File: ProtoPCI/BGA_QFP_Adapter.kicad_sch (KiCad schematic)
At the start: 2 parts

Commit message: Initial BGA to QFP Adapter for QFP replacement via BGA
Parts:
- U2: footprint Package_QFP:PQFP-160_28x28mm_P0.65mm -> DFT:DFT_PQFP-160_28x28mm_P0.65mm_Adapter
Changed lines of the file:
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@@
 			)
 		)
-		(property "Footprint" "Package_QFP:PQFP-160_28x28mm_P0.65mm"
+		(property "Footprint" "DFT:DFT_PQFP-160_28x28mm_P0.65mm_Adapter"
 			(at 147.32 92.71 0)
 			(effects

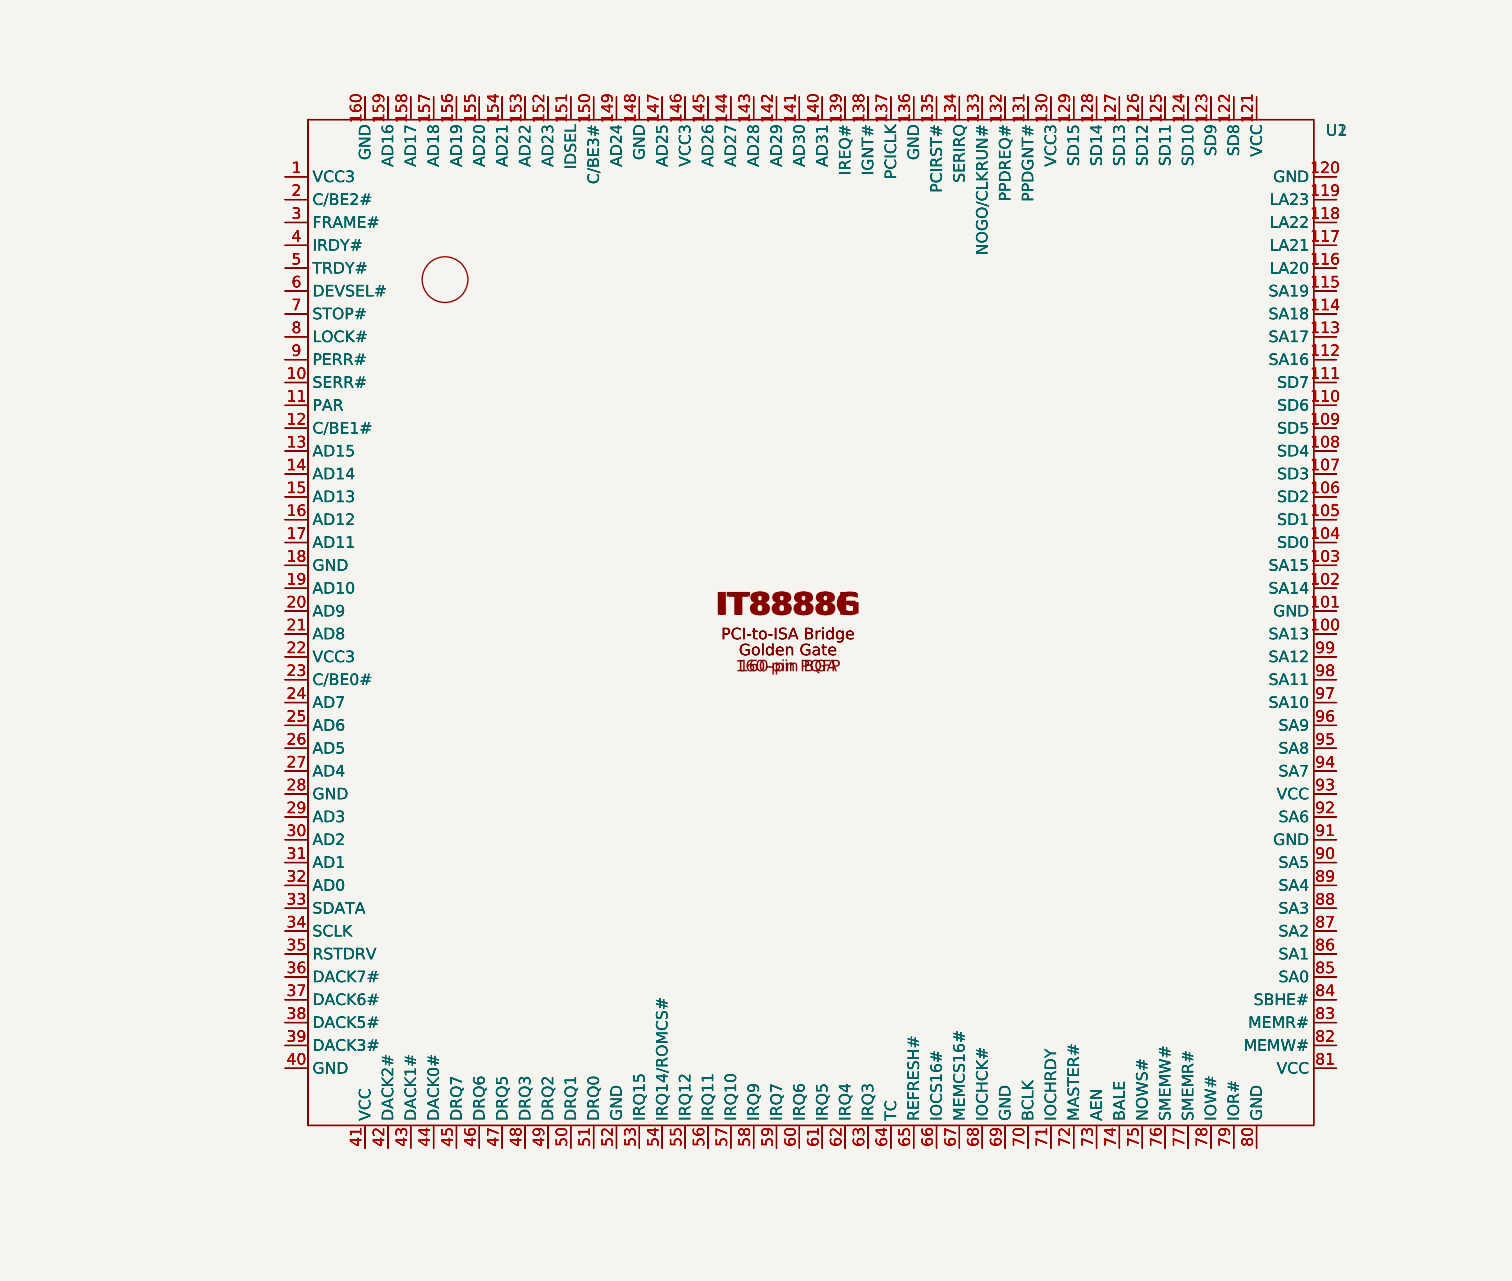
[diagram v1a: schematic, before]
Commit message: BGA/QFP Adapter Setup
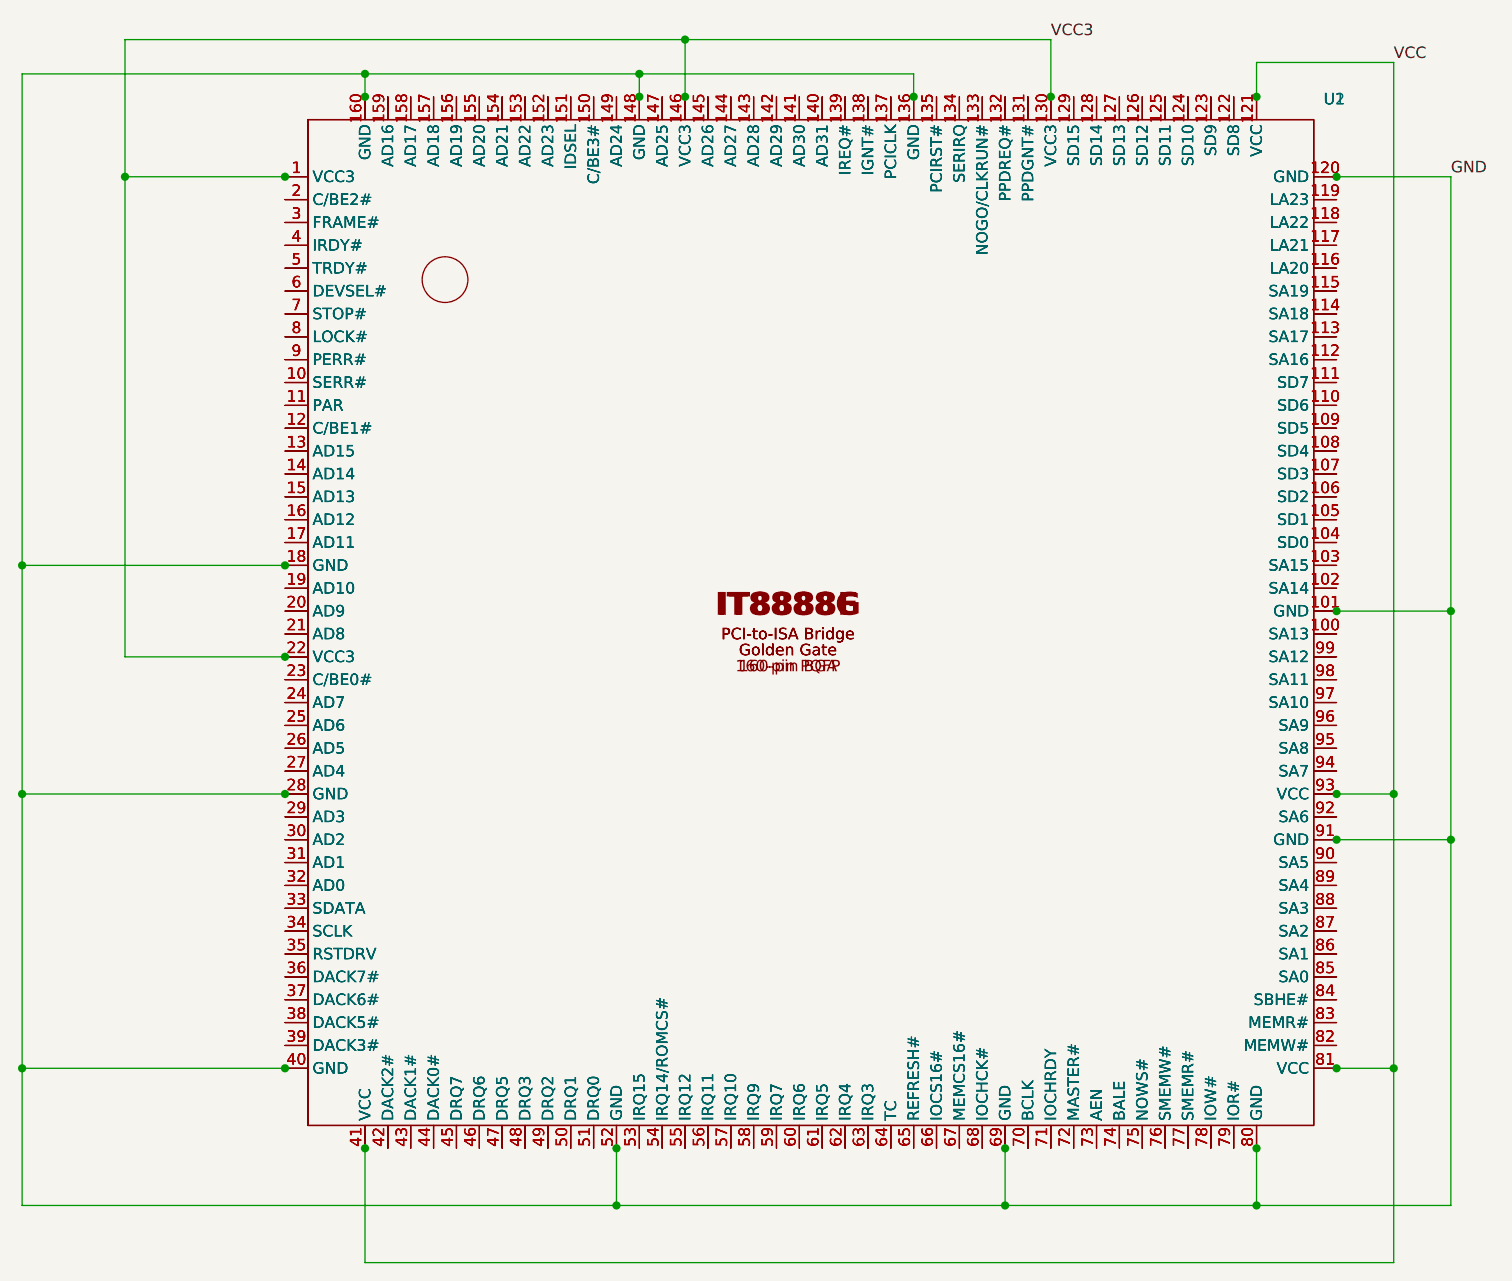
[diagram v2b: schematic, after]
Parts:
- U1: footprint DFT:IT8888G -> DFT:IT8888G_QFP_Naming
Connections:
- net VCC3: now reaches U1.1 (VCC3), U2.1 (VCC3)
- net VCC3: now also U1.130 (VCC3), U1.146 (VCC3), U1.22 (VCC3), U2.130 (VCC3), U2.146 (VCC3), U2.22 (VCC3)
- net GND: now reaches U1.101 (GND), U2.101 (GND)
- net GND: now also U1.120 (GND), U1.136 (GND), U1.148 (GND), U1.160 (GND), U1.18 (GND), U1.28 (GND), U1.40 (GND), U1.52 (GND), U1.69 (GND), U1.80 (GND), U1.91 (GND), U2.120 (GND), U2.136 (GND), U2.148 (GND), U2.160 (GND), U2.18 (GND), U2.28 (GND), U2.40 (GND), U2.52 (GND), U2.69 (GND), U2.80 (GND), U2.91 (GND)
- net VCC: now reaches U1.121 (VCC), U2.121 (VCC)
- net VCC: now also U1.41 (VCC), U1.81 (VCC), U1.93 (VCC), U2.41 (VCC), U2.81 (VCC), U2.93 (VCC)
